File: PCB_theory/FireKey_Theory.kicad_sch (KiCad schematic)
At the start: 0 parts

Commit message: Added 3_LEDs Theory
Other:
- added sheet 3_LEDs_Serial (3_LEDs_Serial.kicad_sch)
- added sheet 3_LEDs_Single (3_LEDs_Single.kicad_sch)
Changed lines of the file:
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@@
+    )
+  )
+  (sheet (at 85.09 24.13) (size 12.7 10.16) (fields_autoplaced)
+    (stroke (width 0.1524) (type solid) (color 0 0 0 0))
+    (fill (color 0 255 0 0.5000))
+    (property "Sheet name" "3_LEDs_Single" (id 0) (at 85.09 23.4184 0)
+      (effects (font (size 1.27 1.27)) (justify left bottom))
+    )
+    (property "Sheet file" "3_LEDs_Single.kicad_sch" (id 1) (at 85.09 34.8746 0)
+      (effects (font (size 1.27 1.27)) (justify left top) hide)
     )
   )
@@
     )
     (property "Sheet file" "1_Button_Single.kicad_sch" (id 1) (at 21.59 34.8746 0)
+      (effects (font (size 1.27 1.27)) (justify left top) hide)
+    )
+  )
+  (sheet (at 85.09 39.37) (size 12.7 10.16) (fields_autoplaced)
+    (stroke (width 0.1524) (type solid) (color 0 0 0 0))
+    (fill (color 0 255 0 0.5000))
+    (property "Sheet name" "3_LEDs_Serial" (id 0) (at 85.09 38.6584 0)
+      (effects (font (size 1.27 1.27)) (justify left bottom))
+    )
+    (property "Sheet file" "3_LEDs_Serial.kicad_sch" (id 1) (at 85.09 50.1146 0)
       (effects (font (size 1.27 1.27)) (justify left top) hide)
     )
@@
     (path "/edf8e0cd-77bf-40bd-91ed-3a57f3e9625c" (page "4"))
     (path "/fea28a73-9216-40e4-baa1-ae6d12b7a60b" (page "5"))
+    (path "/867f5ee4-59cf-4f77-af1a-7b833f6c8402" (page "6"))
+    (path "/23c54e02-1933-44b9-a71b-11c9d678f354" (page "7"))
   )
   (symbol_instances
@@
       (reference "#PWR0109") (unit 1) (value "GND") (footprint "")
     )
+    (path "/867f5ee4-59cf-4f77-af1a-7b833f6c8402/028279b0-3f7f-492d-97fe-10b67d92f285"
+      (reference "#PWR?") (unit 1) (value "VCC") (footprint "")
+    )
+    (path "/867f5ee4-59cf-4f77-af1a-7b833f6c8402/114b0695-4c2c-423a-a3fb-cfa3540ec965"
+      (reference "#PWR?") (unit 1) (value "VCC") (footprint "")
+    )
+    (path "/23c54e02-1933-44b9-a71b-11c9d678f354/586a16e5-b6de-46e1-a856-687262c06536"
+      (reference "#PWR?") (unit 1) (value "VCC") (footprint "")
+    )
+    (path "/867f5ee4-59cf-4f77-af1a-7b833f6c8402/702629f9-d1c7-4431-8d05-ede4bb34a1db"
+      (reference "#PWR?") (unit 1) (value "GND") (footprint "")
+    )
+    (path "/23c54e02-1933-44b9-a71b-11c9d678f354/8a55d35b-9f5c-4c2b-be2e-adc8bb010978"
+      (reference "#PWR?") (unit 1) (value "VCC") (footprint "")
+    )
+    (path "/867f5ee4-59cf-4f77-af1a-7b833f6c8402/a291e06f-8735-4218-97ff-0a8ac88f1d10"
+      (reference "#PWR?") (unit 1) (value "GND") (footprint "")
+    )
+    (path "/23c54e02-1933-44b9-a71b-11c9d678f354/fbc54439-eeb4-4b31-92ed-ad308213d469"
+      (reference "#PWR?") (unit 1) (value "VCC") (footprint "")
+    )
+    (path "/867f5ee4-59cf-4f77-af1a-7b833f6c8402/3a374453-af31-406b-a73f-f39a6475a5ab"
+      (reference "C0") (unit 1) (value "100nF") (footprint "Capacitor_SMD:C_0603_1608Metric_Pad1.08x0.95mm_HandSolder")
+    )
+    (path "/867f5ee4-59cf-4f77-af1a-7b833f6c8402/fecc4ec9-b5f8-4973-9e00-9b45013e5b86"
+      (reference "C1") (unit 1) (value "100nF") (footprint "Capacitor_SMD:C_0603_1608Metric_Pad1.08x0.95mm_HandSolder")
+    )
+    (path "/867f5ee4-59cf-4f77-af1a-7b833f6c8402/39348e89-4cd5-4007-9e6f-4cff738e98c3"
+      (reference "C2") (unit 1) (value "100nF") (footprint "Capacitor_SMD:C_0603_1608Metric_Pad1.08x0.95mm_HandSolder")
+    )
+    (path "/867f5ee4-59cf-4f77-af1a-7b833f6c8402/b6f63e44-668a-4cb1-a28b-2d20d93ae415"
+      (reference "C4") (unit 1) (value "100nF") (footprint "Capacitor_SMD:C_0603_1608Metric_Pad1.08x0.95mm_HandSolder")
+    )
     (path "/fea28a73-9216-40e4-baa1-ae6d12b7a60b/6db4d6f7-2869-4ea4-bbec-ac147de51dd4"
       (reference "D1") (unit 1) (value "1N4148W") (footprint "Custom_Parts:D_SOD-123")
@@
       (reference "D?") (unit 1) (value "1N4148W") (footprint "Custom_Parts:D_SOD-123")
     )
+    (path "/23c54e02-1933-44b9-a71b-11c9d678f354/12dd15cc-d597-4fe3-a37a-b379dc72e1ed"
+      (reference "D?") (unit 1) (value "LED_RGBA") (footprint "")
+    )
     (path "/edf8e0cd-77bf-40bd-91ed-3a57f3e9625c/34136bee-ccea-4c59-b5e1-e582f82ee9d5"
       (reference "D?") (unit 1) (value "1N4148W") (footprint "Custom_Parts:D_SOD-123")
@@
       (reference "D?") (unit 1) (value "1N4148W") (footprint "Custom_Parts:D_SOD-123")
     )
+    (path "/23c54e02-1933-44b9-a71b-11c9d678f354/58dea942-7c3a-4ca0-bc12-95c5b8a61fc3"
+      (reference "D?") (unit 1) (value "LED_RGBA") (footprint "")
+    )
     (path "/edf8e0cd-77bf-40bd-91ed-3a57f3e9625c/599a9b18-5938-47b2-986e-386a45392b85"
       (reference "D?") (unit 1) (value "1N4148W") (footprint "Custom_Parts:D_SOD-123")
@@
     (path "/edf8e0cd-77bf-40bd-91ed-3a57f3e9625c/611fe2a0-e800-4eb1-83d9-e95309baf7d8"
       (reference "D?") (unit 1) (value "1N4148W") (footprint "Custom_Parts:D_SOD-123")
+    )
+    (path "/23c54e02-1933-44b9-a71b-11c9d678f354/68efbed4-9638-4cad-8668-c2f633284908"
+      (reference "D?") (unit 1) (value "LED_RGBA") (footprint "")
     )
     (path "/edf8e0cd-77bf-40bd-91ed-3a57f3e9625c/e61754db-02af-4e9d-9bb2-17d15f3dd7da"
@@
       (reference "KEY15") (unit 1) (value "SW_MX") (footprint "Custom_Parts:SW_Cherry_MX_1.00u_PCB_CleanFront")
     )
+    (path "/867f5ee4-59cf-4f77-af1a-7b833f6c8402/f74bb2c2-e2b9-4749-97fc-d2f3417390e6"
+      (reference "LED0") (unit 1) (value "SK6812") (footprint "Custom_Parts:DY-S352818-6812-2T")
+    )
+    (path "/867f5ee4-59cf-4f77-af1a-7b833f6c8402/1981aac3-38d3-46d7-85c5-41a11f44f34c"
+      (reference "LED1") (unit 1) (value "SK6812") (footprint "Custom_Parts:DY-S352818-6812-2T")
+    )
+    (path "/867f5ee4-59cf-4f77-af1a-7b833f6c8402/7dacd14c-8fb1-4045-8f06-f8714a6ae5db"
+      (reference "LED2") (unit 1) (value "SK6812") (footprint "Custom_Parts:DY-S352818-6812-2T")
+    )
+    (path "/867f5ee4-59cf-4f77-af1a-7b833f6c8402/345b632f-44f2-4e0b-9a2a-6e8673c28e47"
+      (reference "LED4") (unit 1) (value "SK6812") (footprint "Custom_Parts:DY-S352818-6812-2T")
+    )
+    (path "/867f5ee4-59cf-4f77-af1a-7b833f6c8402/524b9dc4-a455-4e5a-9db4-40cf8f3c2530"
+      (reference "R1") (unit 1) (value "470") (footprint "Resistor_SMD:R_0603_1608Metric_Pad0.98x0.95mm_HandSolder")
+    )
     (path "/5796d21e-c689-47f8-a795-b681878fc3f0/1d6b2a96-dd6d-4a75-9586-733fd6f3254b"

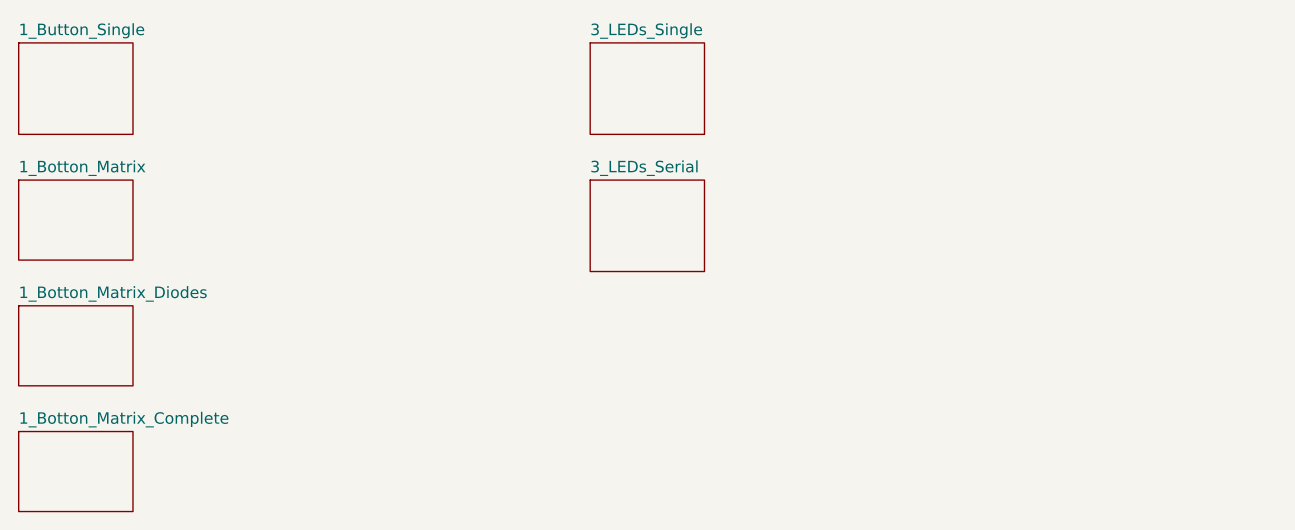
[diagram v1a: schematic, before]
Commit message: added 3_LEDs_complete
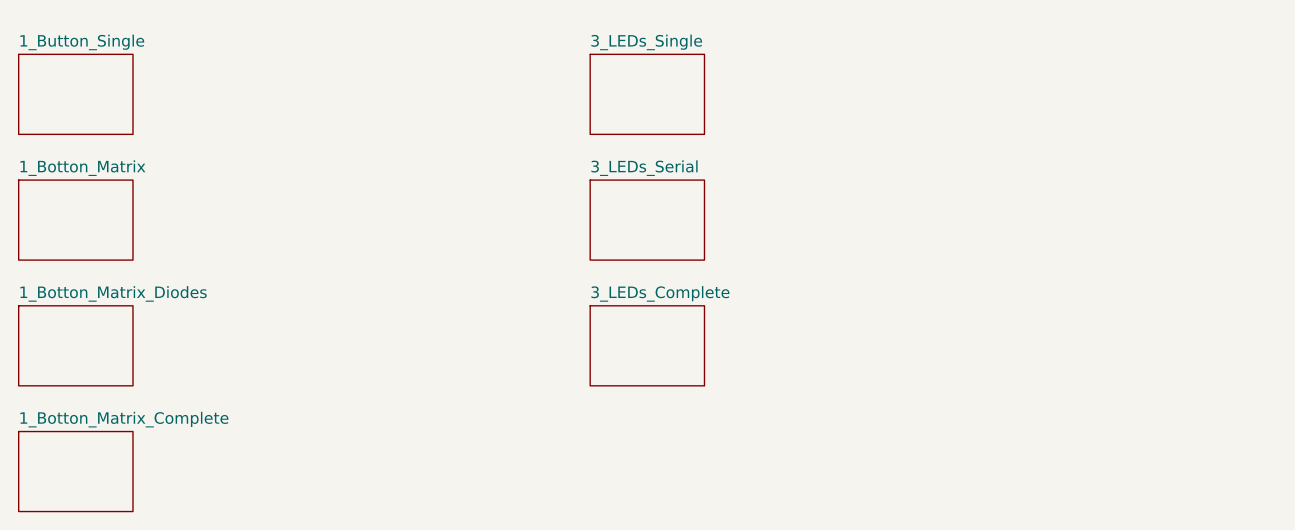
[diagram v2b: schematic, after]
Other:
- added sheet 3_LEDs_Complete (3_LEDs_Complete.kicad_sch)

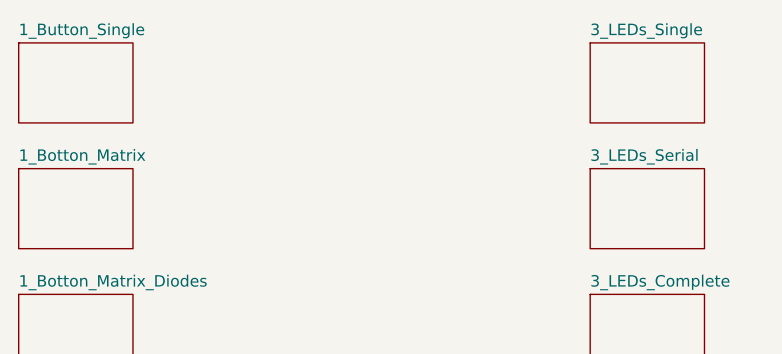
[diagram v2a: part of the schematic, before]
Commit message: added 2_oled
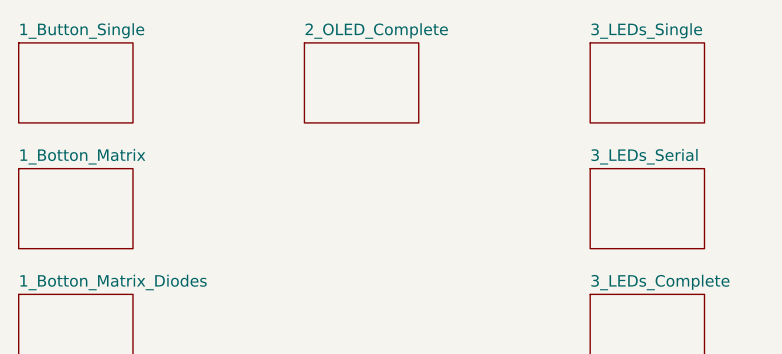
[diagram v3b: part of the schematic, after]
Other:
- added sheet 2_OLED_Complete (2_OLED_Complete.kicad_sch)
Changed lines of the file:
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@@
+    )
+  )
+  (sheet (at 53.34 25.4) (size 12.7 8.89) (fields_autoplaced)
+    (stroke (width 0.1524) (type solid) (color 0 0 0 0))
+    (fill (color 0 0 255 0.5000))
+    (property "Sheet name" "2_OLED_Complete" (id 0) (at 53.34 24.6884 0)
+      (effects (font (size 1.27 1.27)) (justify left bottom))
+    )
+    (property "Sheet file" "2_OLED_Complete.kicad_sch" (id 1) (at 53.34 34.8746 0)
+      (effects (font (size 1.27 1.27)) (justify left top) hide)
     )
   )
@@
     (path "/23c54e02-1933-44b9-a71b-11c9d678f354" (page "7"))
     (path "/be4fbbf8-ca7b-4e15-bf90-f58e61bbadbc" (page "8"))
+    (path "/8cb60a14-ef8a-44df-a0e8-c62f829ba9cb" (page "9"))
   )
   (symbol_instances
@@
       (reference "#PWR?") (unit 1) (value "VCC") (footprint "")
     )
+    (path "/8cb60a14-ef8a-44df-a0e8-c62f829ba9cb/03073b22-b733-4351-b56e-dab8c6c937c2"
+      (reference "#PWR?") (unit 1) (value "VCC") (footprint "")
+    )
+    (path "/8cb60a14-ef8a-44df-a0e8-c62f829ba9cb/09be9e90-f823-4835-9a83-d2883bd9cbe4"
+      (reference "#PWR?") (unit 1) (value "VCC") (footprint "")
+    )
     (path "/867f5ee4-59cf-4f77-af1a-7b833f6c8402/114b0695-4c2c-423a-a3fb-cfa3540ec965"
       (reference "#PWR?") (unit 1) (value "VCC") (footprint "")
     )
+    (path "/8cb60a14-ef8a-44df-a0e8-c62f829ba9cb/193d50ae-8c4f-4890-9de4-7cd4a9746aab"
+      (reference "#PWR?") (unit 1) (value "GND") (footprint "")
+    )
     (path "/be4fbbf8-ca7b-4e15-bf90-f58e61bbadbc/2ed61c47-4a2d-44bc-be53-3352afe34322"
       (reference "#PWR?") (unit 1) (value "GND") (footprint "")
@@
     (path "/be4fbbf8-ca7b-4e15-bf90-f58e61bbadbc/6cbffdaf-167d-40e2-8568-7c5ed9b53b61"
       (reference "#PWR?") (unit 1) (value "VCC") (footprint "")
+    )
+    (path "/8cb60a14-ef8a-44df-a0e8-c62f829ba9cb/6d46e50b-a506-4d0f-a8fb-d1bb8e4fb5c3"
+      (reference "#PWR?") (unit 1) (value "GND") (footprint "")
     )
     (path "/867f5ee4-59cf-4f77-af1a-7b833f6c8402/702629f9-d1c7-4431-8d05-ede4bb34a1db"
@@
       (reference "LED14") (unit 1) (value "SK6812") (footprint "Custom_Parts:DY-S352818-6812-2T")
     )
+    (path "/8cb60a14-ef8a-44df-a0e8-c62f829ba9cb/d1ff457c-8822-4e4a-aded-30b946759504"
+      (reference "OLED?") (unit 1) (value "OLED_1.3_4P_GV") (footprint "Custom_Module:OLED_1.3_4P_M2.5Holes_CleanFront")
+    )
+    (path "/8cb60a14-ef8a-44df-a0e8-c62f829ba9cb/e58e319f-122a-49ea-9985-2d1669a943bc"
+      (reference "OLED?") (unit 1) (value "OLED_1.3_4P_GV") (footprint "Custom_Module:OLED_1.3_4P_M2.5Holes_CleanFront")
+    )
     (path "/867f5ee4-59cf-4f77-af1a-7b833f6c8402/524b9dc4-a455-4e5a-9db4-40cf8f3c2530"

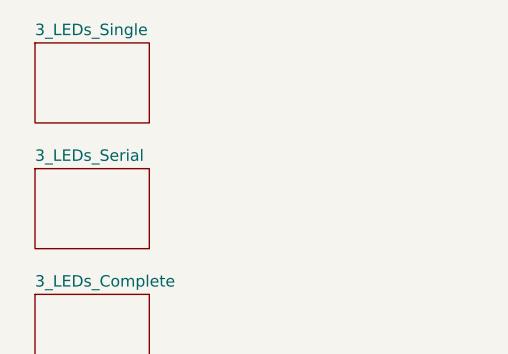
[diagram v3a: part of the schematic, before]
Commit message: added 4_mcu to theory
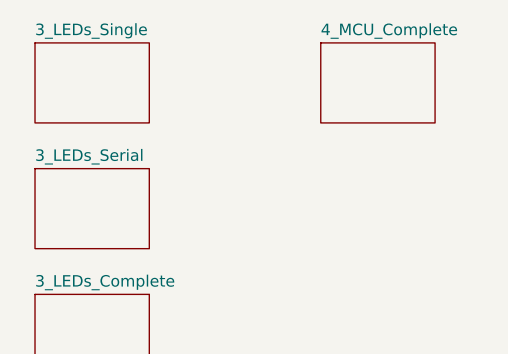
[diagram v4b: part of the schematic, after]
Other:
- added sheet 4_MCU_Complete (4_MCU_Complete.kicad_sch)
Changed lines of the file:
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@@
+    )
+  )
+  (sheet (at 116.84 25.4) (size 12.7 8.89) (fields_autoplaced)
+    (stroke (width 0.1524) (type solid) (color 0 0 0 0))
+    (fill (color 255 0 255 0.5000))
+    (property "Sheet name" "4_MCU_Complete" (id 0) (at 116.84 24.6884 0)
+      (effects (font (size 1.27 1.27)) (justify left bottom))
+    )
+    (property "Sheet file" "4_MCU_Complete.kicad_sch" (id 1) (at 116.84 34.8746 0)
+      (effects (font (size 1.27 1.27)) (justify left top) hide)
     )
   )
@@
     (path "/be4fbbf8-ca7b-4e15-bf90-f58e61bbadbc" (page "8"))
     (path "/8cb60a14-ef8a-44df-a0e8-c62f829ba9cb" (page "9"))
+    (path "/262cdc52-6401-4bb3-8d5f-c46b612bd77a" (page "10"))
   )
   (symbol_instances
@@
       (reference "#PWR?") (unit 1) (value "GND") (footprint "")
     )
+    (path "/262cdc52-6401-4bb3-8d5f-c46b612bd77a/2f32e398-bdc6-4fe4-a01c-53049449f922"
+      (reference "#PWR?") (unit 1) (value "GND") (footprint "")
+    )
     (path "/23c54e02-1933-44b9-a71b-11c9d678f354/586a16e5-b6de-46e1-a856-687262c06536"
       (reference "#PWR?") (unit 1) (value "VCC") (footprint "")
@@
       (reference "#PWR?") (unit 1) (value "GND") (footprint "")
     )
+    (path "/262cdc52-6401-4bb3-8d5f-c46b612bd77a/6f0e2a8a-e91d-4576-a886-6d37d4bbba97"
+      (reference "#PWR?") (unit 1) (value "VCC") (footprint "")
+    )
     (path "/867f5ee4-59cf-4f77-af1a-7b833f6c8402/702629f9-d1c7-4431-8d05-ede4bb34a1db"
       (reference "#PWR?") (unit 1) (value "GND") (footprint "")
@@
       (reference "#PWR?") (unit 1) (value "GND") (footprint "")
     )
+    (path "/262cdc52-6401-4bb3-8d5f-c46b612bd77a/b1d91dd3-abe4-4c31-a968-0f23ce233707"
+      (reference "#PWR?") (unit 1) (value "GND") (footprint "")
+    )
     (path "/be4fbbf8-ca7b-4e15-bf90-f58e61bbadbc/b7e7aacd-beba-4542-8aaf-946245714f16"
       (reference "#PWR?") (unit 1) (value "VCC") (footprint "")
     )
     (path "/be4fbbf8-ca7b-4e15-bf90-f58e61bbadbc/c1de2571-1167-4aa4-b1bd-3ceba2ee053c"
+      (reference "#PWR?") (unit 1) (value "GND") (footprint "")
+    )
+    (path "/262cdc52-6401-4bb3-8d5f-c46b612bd77a/cb8f9b64-6c2f-4c95-b87a-01dd6fa5192d"
       (reference "#PWR?") (unit 1) (value "GND") (footprint "")
     )
@@
     )
     (path "/8cb60a14-ef8a-44df-a0e8-c62f829ba9cb/d1ff457c-8822-4e4a-aded-30b946759504"
-      (reference "OLED?") (unit 1) (value "OLED_1.3_4P_GV") (footprint "Custom_Module:OLED_1.3_4P_M2.5Holes_CleanFront")
+      (reference "OLED1") (unit 1) (value "OLED_1.3_4P_GV") (footprint "Custom_Module:OLED_1.3_4P_M2.5Holes_CleanFront")
     )
     (path "/8cb60a14-ef8a-44df-a0e8-c62f829ba9cb/e58e319f-122a-49ea-9985-2d1669a943bc"
-      (reference "OLED?") (unit 1) (value "OLED_1.3_4P_GV") (footprint "Custom_Module:OLED_1.3_4P_M2.5Holes_CleanFront")
+      (reference "OLED2") (unit 1) (value "OLED_1.3_4P_GV") (footprint "Custom_Module:OLED_1.3_4P_M2.5Holes_CleanFront")
     )
     (path "/867f5ee4-59cf-4f77-af1a-7b833f6c8402/524b9dc4-a455-4e5a-9db4-40cf8f3c2530"
@@
       (reference "SW?") (unit 1) (value "SW_SPST") (footprint "")
     )
-  )
+    (path "/262cdc52-6401-4bb3-8d5f-c46b612bd77a/4959e9d8-e2fa-409d-9377-5b188ba05792"
+      (reference "U1") (unit 1) (value "Arduino_Pro_Micro_USB-C") (footprint "Custom_MCU:Arduino_Pro_Micro_USB-C_CleanFront")
+    )
+  )

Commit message: added 5_bouce to theory
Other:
- added sheet 5_Bounce (5_Bounce.kicad_sch)
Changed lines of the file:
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@@
+    )
+  )
+  (sheet (at 148.59 25.4) (size 12.7 8.89) (fields_autoplaced)
+    (stroke (width 0.1524) (type solid) (color 0 0 0 0))
+    (fill (color 0 0 0 0.5000))
+    (property "Sheet name" "5_Bounce" (id 0) (at 148.59 24.6884 0)
+      (effects (font (size 1.27 1.27)) (justify left bottom))
+    )
+    (property "Sheet file" "5_Bounce.kicad_sch" (id 1) (at 148.59 34.8746 0)
+      (effects (font (size 1.27 1.27)) (justify left top) hide)
     )
   )
@@
     (path "/8cb60a14-ef8a-44df-a0e8-c62f829ba9cb" (page "9"))
     (path "/262cdc52-6401-4bb3-8d5f-c46b612bd77a" (page "10"))
+    (path "/023a82a5-dc98-40ff-97a4-4af55166cbb8" (page "11"))
   )
   (symbol_instances
@@
       (reference "#PWR?") (unit 1) (value "GND") (footprint "")
     )
+    (path "/023a82a5-dc98-40ff-97a4-4af55166cbb8/45c6e1ef-4cbf-4962-8196-d3df3bf65266"
+      (reference "#PWR?") (unit 1) (value "GND") (footprint "")
+    )
     (path "/23c54e02-1933-44b9-a71b-11c9d678f354/586a16e5-b6de-46e1-a856-687262c06536"
       (reference "#PWR?") (unit 1) (value "VCC") (footprint "")
@@
       (reference "#PWR?") (unit 1) (value "VCC") (footprint "")
     )
+    (path "/023a82a5-dc98-40ff-97a4-4af55166cbb8/6be91483-6bb0-4285-ad0b-e21e9d8d1497"
+      (reference "#PWR?") (unit 1) (value "VCC") (footprint "")
+    )
     (path "/be4fbbf8-ca7b-4e15-bf90-f58e61bbadbc/6cbffdaf-167d-40e2-8568-7c5ed9b53b61"
       (reference "#PWR?") (unit 1) (value "VCC") (footprint "")
@@
     (path "/be4fbbf8-ca7b-4e15-bf90-f58e61bbadbc/91785aeb-3fe9-4d65-a5b9-c77ce13762a2"
       (reference "#PWR?") (unit 1) (value "GND") (footprint "")
+    )
+    (path "/023a82a5-dc98-40ff-97a4-4af55166cbb8/9ecf534d-29b7-4061-bf7c-51deced1d19e"
+      (reference "#PWR?") (unit 1) (value "VCC") (footprint "")
     )
     (path "/be4fbbf8-ca7b-4e15-bf90-f58e61bbadbc/9f0d7e28-a779-430e-9bab-e1c6a4326f41"
@@
       (reference "R1") (unit 1) (value "470") (footprint "Resistor_SMD:R_0603_1608Metric_Pad0.98x0.95mm_HandSolder")
     )
+    (path "/023a82a5-dc98-40ff-97a4-4af55166cbb8/4f1a195a-30ff-447d-9ccf-5335c8e453ae"
+      (reference "R?") (unit 1) (value "R") (footprint "")
+    )
+    (path "/023a82a5-dc98-40ff-97a4-4af55166cbb8/8c5ff4b1-97d7-40ad-aed4-7704c123e9df"
+      (reference "R?") (unit 1) (value "R") (footprint "")
+    )
     (path "/5796d21e-c689-47f8-a795-b681878fc3f0/1d6b2a96-dd6d-4a75-9586-733fd6f3254b"
       (reference "SW?") (unit 1) (value "SW_SPST") (footprint "")
@@
     (path "/5796d21e-c689-47f8-a795-b681878fc3f0/a1b098d4-3f9b-40db-9262-df3a76e030d3"
       (reference "SW?") (unit 1) (value "SW_SPST") (footprint "")
+    )
+    (path "/023a82a5-dc98-40ff-97a4-4af55166cbb8/ab33547f-2b9f-4764-a62a-4a7614c1f186"
+      (reference "SW?") (unit 1) (value "SW_SPDT") (footprint "")
     )
     (path "/5796d21e-c689-47f8-a795-b681878fc3f0/c1ed7e49-83c7-4caa-b494-15411e384ee9"
@@
       (reference "U1") (unit 1) (value "Arduino_Pro_Micro_USB-C") (footprint "Custom_MCU:Arduino_Pro_Micro_USB-C_CleanFront")
     )
-  )
+    (path "/023a82a5-dc98-40ff-97a4-4af55166cbb8/c7a9a4fb-0cd3-4d11-a41a-1d8727accfbd"
+      (reference "U?") (unit 1) (value "74LS00") (footprint "")
+    )
+    (path "/023a82a5-dc98-40ff-97a4-4af55166cbb8/03bef755-1605-44bc-85a1-b8d4e201a7cd"
+      (reference "U?") (unit 2) (value "74LS00") (footprint "")
+    )
+  )
